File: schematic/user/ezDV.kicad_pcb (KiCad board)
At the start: 4 copper layers, 64.8 x 69.9 mm, 92 parts, among them J1 TYPE-C-31-M-04, J2 Radio_Jack, J3 User_Jack, J4 I2C Breakout, J5 PTT Breakout, Q1 AO3401A, Q2 AO3401A, Q3 MBT3904DW1T1, Q4 MBT3904DW1T1, Q5 MBT3904DW1T1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

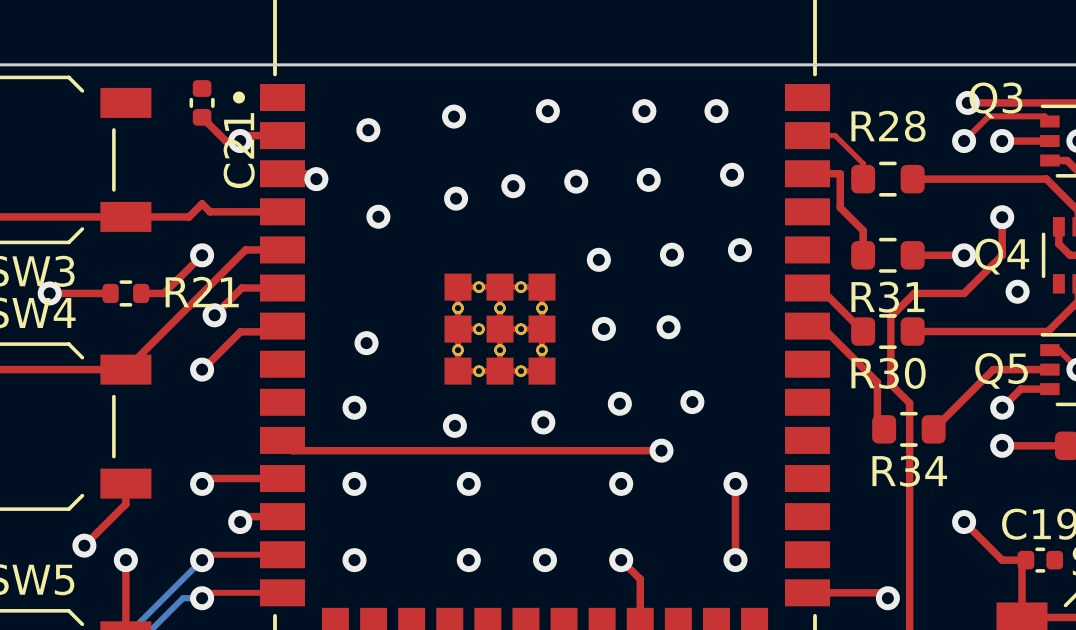
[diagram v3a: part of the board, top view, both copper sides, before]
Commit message: v0.5 board: move PTT and NET GPIOs to RTC domain.
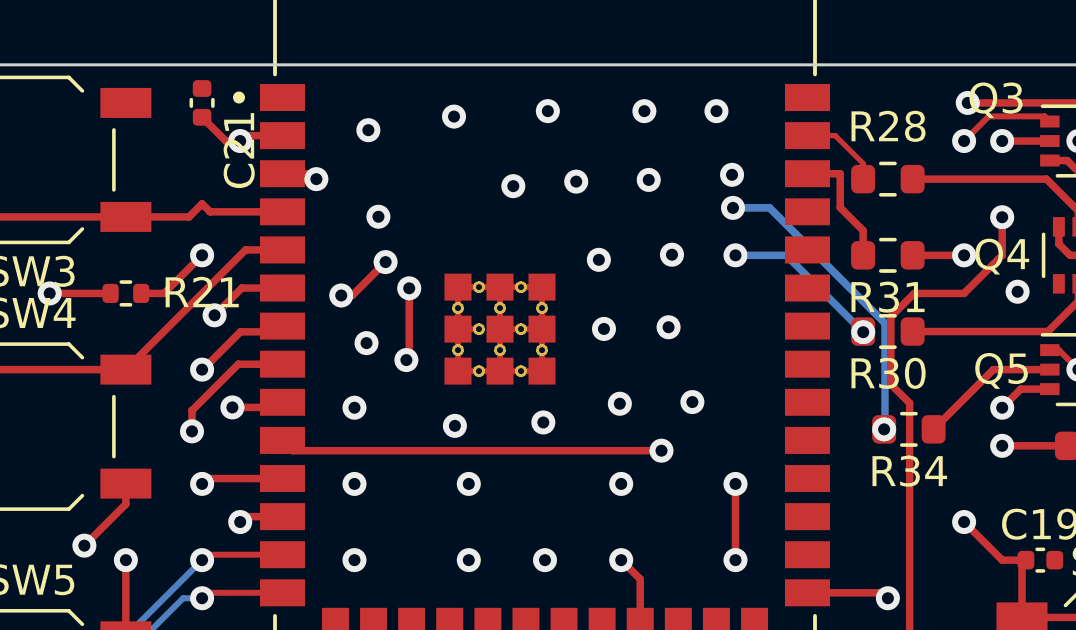
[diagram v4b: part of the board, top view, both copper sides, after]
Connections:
- R30 pad 2: GPIO42_NET_LED -> GPIO16_NET_LED
- R34 pad 2: GPIO41_PTT_LED -> GPIO15_PTT_LED
- U5 pad 34: GPIO41_PTT_LED -> unconnected-(U5-Pad34)
- U5 pad 35: GPIO42_NET_LED -> unconnected-(U5-Pad35)
- U5 pad 8: unconnected-(U5-Pad8) -> GPIO15_PTT_LED
- U5 pad 9: unconnected-(U5-Pad9) -> GPIO16_NET_LED
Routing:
- net GPIO15_PTT_LED: track 0.00 -> 36.0 mm, vias 0 -> 5
- net GPIO16_NET_LED: track 0.00 -> 28.2 mm, vias 0 -> 5
- net GPIO41_PTT_LED: track 4.77 -> 0.00 mm
- net GPIO42_NET_LED: track 2.46 -> 0.00 mm
- net GND: vias 237 -> 235
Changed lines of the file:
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@@
   (net 71 "GPIO7_VOL_DOWN")
   (net 72 "GPIO1_SYNC_LED")
-  (net 73 "GPIO42_NET_LED")
+  (net 73 "GPIO16_NET_LED")
   (net 74 "GPIO2_OVL_LED")
-  (net 75 "GPIO41_PTT_LED")
+  (net 75 "GPIO15_PTT_LED")
   (net 76 "GPIO0_BOOT")
   (net 77 "GPIO8_BAT_ALERT")
-  (net 78 "unconnected-(U5-Pad9)")
+  (net 78 "unconnected-(U5-Pad34)")
   (net 79 "GPIO17_PERIPH_PWR")
   (net 80 "unconnected-(J1-PadS1)")
@@
   (net 96 "TP4056_NTC")
   (net 97 "GPIO18_BOARD_TEMP")
-  (net 98 "unconnected-(U5-Pad8)")
+  (net 98 "unconnected-(U5-Pad35)")
   (net 99 "unconnected-(U5-Pad25)")
   (footprint "Resistor_SMD:R_0603_1608Metric" (layer "F.Cu")
@@
       (net 49 "Net-(Q4-Pad5)") (pintype "passive"))
     (pad "2" smd roundrect (at 0.825 0 180) (size 0.8 0.95) (layers "F.Cu" "F.Paste" "F.Mask") (roundrect_rratio 0.25)
-      (net 73 "GPIO42_NET_LED") (pintype "passive"))
+      (net 73 "GPIO16_NET_LED") (pintype "passive"))
     (model "${KICAD6_3DMODEL_DIR}/Resistor_SMD.3dshapes/R_0603_1608Metric.wrl"
       (offset (xyz 0 0 0))
@@
       (net 71 "GPIO7_VOL_DOWN") (pinfunction "IO7") (pintype "bidirectional"))
     (pad "8" smd rect locked (at -8.75 3.63) (size 1.5 0.9) (layers "F.Cu" "F.Paste" "F.Mask")
-      (net 98 "unconnected-(U5-Pad8)") (pinfunction "IO15") (pintype "bidirectional+no_connect"))
+      (net 75 "GPIO15_PTT_LED") (pinfunction "IO15") (pintype "bidirectional"))
     (pad "9" smd rect locked (at -8.75 4.9) (size 1.5 0.9) (layers "F.Cu" "F.Paste" "F.Mask")
-      (net 78 "unconnected-(U5-Pad9)") (pinfunction "IO16") (pintype "bidirectional+no_connect"))
+      (net 73 "GPIO16_NET_LED") (pinfunction "IO16") (pintype "bidirectional"))
     (pad "10" smd rect locked (at -8.75 6.17) (size 1.5 0.9) (layers "F.Cu" "F.Paste" "F.Mask")
       (net 79 "GPIO17_PERIPH_PWR") (pinfunction "IO17") (pintype "bidirectional"))
@@
       (net 95 "unconnected-(U5-Pad33)") (pinfunction "IO40") (pintype "bidirectional+no_connect"))
     (pad "34" smd rect locked (at 8.75 2.36) (size 1.5 0.9) (layers "F.Cu" "F.Paste" "F.Mask")
-      (net 75 "GPIO41_PTT_LED") (pinfunction "IO41") (pintype "bidirectional"))
+      (net 78 "unconnected-(U5-Pad34)") (pinfunction "IO41") (pintype "bidirectional+no_connect"))
     (pad "35" smd rect locked (at 8.75 1.09) (size 1.5 0.9) (layers "F.Cu" "F.Paste" "F.Mask")
-      (net 73 "GPIO42_NET_LED") (pinfunction "IO42") (pintype "bidirectional"))
+      (net 98 "unconnected-(U5-Pad35)") (pinfunction "IO42") (pintype "bidirectional+no_connect"))
     (pad "36" smd rect locked (at 8.75 -0.18) (size 1.5 0.9) (layers "F.Cu" "F.Paste" "F.Mask")
       (net 86 "unconnected-(U5-Pad36)") (pinfunction "RXD0") (pintype "bidirectional+no_connect"))
@@
       (net 50 "Net-(Q5-Pad2)") (pintype "passive"))
     (pad "2" smd roundrect (at 0.825 0 180) (size 0.8 0.95) (layers "F.Cu" "F.Paste" "F.Mask") (roundrect_rratio 0.25)
-      (net 75 "GPIO41_PTT_LED") (pintype "passive"))
+      (net 75 "GPIO15_PTT_LED") (pintype "passive"))
     (model "${KICAD6_3DMODEL_DIR}/Resistor_SMD.3dshapes/R_0603_1608Metric.wrl"
       (offset (xyz 0 0 0))
@@
   (via (at 90.17 107.95) (size 0.8) (drill 0.4) (layers "F.Cu" "B.Cu") (free) (net 2))
   (via (at 82.329331 117.655234) (size 0.8) (drill 0.4) (layers "F.Cu" "B.Cu") (free) (net 2))
-  (via (at 80.159472 74.758624) (size 0.8) (drill 0.4) (layers "F.Cu" "B.Cu") (free) (net 2))
   (via (at 47.324831 88.987026) (size 0.8) (drill 0.4) (layers "F.Cu" "B.Cu") (free) (net 2))
   (via (at 104.265111 94.610548) (size 0.8) (drill 0.4) (layers "F.Cu" "B.Cu") (free) (net 2))
@@
   (via (at 95.184712 114.038378) (size 0.8) (drill 0.4) (layers "F.Cu" "B.Cu") (free) (net 2))
   (via (at 55.88 105.41) (size 0.8) (drill 0.4) (layers "F.Cu" "B.Cu") (free) (net 2))
-  (via (at 70.695662 73.039648) (size 0.8) (drill 0.4) (layers "F.Cu" "B.Cu") (free) (net 2))
   (via (at 76.179226 132.09359) (size 0.8) (drill 0.4) (layers "F.Cu" "B.Cu") (free) (net 2))
   (via (at 92.944297 122.664323) (size 0.8) (drill 0.4) (layers "F.Cu" "B.Cu") (free) (net 2))
@@
   (segment (start 83.335 70.94) (end 84.265 71.87) (width 0.175) (layer "F.Cu") (net 72))
   (segment (start 82.41 70.94) (end 83.335 70.94) (width 0.175) (layer "F.Cu") (net 72))
-  (segment (start 82.815 76.02) (end 84.265 77.47) (width 0.25) (layer "F.Cu") (net 73))
-  (segment (start 82.41 76.02) (end 82.815 76.02) (width 0.25) (layer "F.Cu") (net 73))
+  (segment (start 64.739894 80.000106) (end 64.91 79.83) (width 0.25) (layer "F.Cu") (net 73))
+  (segment (start 69.133734 76.029615) (end 69.133734 78.327485) (width 0.25) (layer "F.Cu") (net 73))
+  (segment (start 63.240008 80.000106) (end 64.739894 80.000106) (width 0.25) (layer "F.Cu") (net 73))
+  (segment (start 69.133734 78.327485) (end 69.039738 78.421481) (width 0.25) (layer "F.Cu") (net 73))
+  (via (at 80.01 74.93) (size 0.8) (drill 0.4) (layers "F.Cu" "B.Cu") (free) (net 73))
+  (via (at 84.267299 77.492096) (size 0.8) (drill 0.4) (layers "F.Cu" "B.Cu") (net 73))
+  (via (at 69.133734 76.029615) (size 0.8) (drill 0.4) (layers "F.Cu" "B.Cu") (free) (net 73))
+  (via (at 69.039738 78.421481) (size 0.8) (drill 0.4) (layers "F.Cu" "B.Cu") (net 73))
+  (via (at 63.240008 80.000106) (size 0.8) (drill 0.4) (layers "F.Cu" "B.Cu") (free) (net 73))
+  (segment (start 69.133734 75.539111) (end 70.488102 74.184743) (width 0.25) (layer "In2.Cu") (net 73))
+  (segment (start 80.01 74.93) (end 79.390017 74.93) (width 0.25) (layer "In2.Cu") (net 73))
+  (segment (start 63.955114 79.285) (end 68.176219 79.285) (width 0.25) (layer "In2.Cu") (net 73))
+  (segment (start 63.240008 80.000106) (end 63.955114 79.285) (width 0.25) (layer "In2.Cu") (net 73))
+  (segment (start 70.488102 74.184743) (end 78.64476 74.184743) (width 0.25) (layer "In2.Cu") (net 73))
+  (segment (start 68.176219 79.285) (end 69.039738 78.421481) (width 0.25) (layer "In2.Cu") (net 73))
+  (segment (start 69.133734 76.029615) (end 69.133734 75.539111) (width 0.25) (layer "In2.Cu") (net 73))
+  (segment (start 79.390017 74.93) (end 78.64476 74.184743) (width 0.25) (layer "In2.Cu") (net 73))
+  (segment (start 80.01 74.93) (end 81.705203 74.93) (width 0.25) (layer "B.Cu") (net 73))
+  (segment (start 81.705203 74.93) (end 84.267299 77.492096) (width 0.25) (layer "B.Cu") (net 73))
   (segment (start 83.501636 72.21) (end 83.501636 73.341636) (width 0.25) (layer "F.Cu") (net 74))
   (segment (start 83.501636 73.341636) (end 84.265 74.105) (width 0.25) (layer "F.Cu") (net 74))
   (segment (start 82.41 72.21) (end 83.501636 72.21) (width 0.25) (layer "F.Cu") (net 74))
   (segment (start 84.265 74.105) (end 84.265 74.93) (width 0.25) (layer "F.Cu") (net 74))
-  (segment (start 82.41 77.29) (end 82.867538 77.29) (width 0.25) (layer "F.Cu") (net 75))
-  (segment (start 82.867538 77.29) (end 84.74 79.162462) (width 0.25) (layer "F.Cu") (net 75))
-  (segment (start 84.74 79.162462) (end 84.74 80.505778) (width 0.25) (layer "F.Cu") (net 75))
-  (segment (start 84.74 80.505778) (end 84.964769 80.730547) (width 0.25) (layer "F.Cu") (net 75))
+  (segment (start 67.233679 76.268467) (end 68.346848 75.155298) (width 0.25) (layer "F.Cu") (net 75))
+  (segment (start 63.435305 78.56) (end 61.89333 80.101975) (width 0.25) (layer "F.Cu") (net 75))
+  (segment (start 66.868292 76.268467) (end 67.233679 76.268467) (width 0.25) (layer "F.Cu") (net 75))
+  (segment (start 61.89333 80.101975) (end 61.89333 80.798493) (width 0.25) (layer "F.Cu") (net 75))
+  (segment (start 64.91 78.56) (end 63.435305 78.56) (width 0.25) (layer "F.Cu") (net 75))
+  (via (at 66.868292 76.268467) (size 0.8) (drill 0.4) (layers "F.Cu" "B.Cu") (net 75))
+  (via (at 79.926698 73.349072) (size 0.8) (drill 0.4) (layers "F.Cu" "B.Cu") (net 75))
+  (via (at 84.964769 80.730547) (size 0.8) (drill 0.4) (layers "F.Cu" "B.Cu") (net 75))
+  (via (at 61.89333 80.798493) (size 0.8) (drill 0.4) (layers "F.Cu" "B.Cu") (free) (net 75))
+  (via (at 68.346848 75.155298) (size 0.8) (drill 0.4) (layers "F.Cu" "B.Cu") (net 75))
+  (segment (start 70.153074 73.349072) (end 79.926698 73.349072) (width 0.25) (layer "In2.Cu") (net 75))
+  (segment (start 68.346848 75.155298) (end 70.153074 73.349072) (width 0.25) (layer "In2.Cu") (net 75))
+  (segment (start 61.89333 80.798493) (end 61.89333 80.321479) (width 0.25) (layer "In2.Cu") (net 75))
+  (segment (start 65.946342 76.268467) (end 66.868292 76.268467) (width 0.25) (layer "In2.Cu") (net 75))
+  (segment (start 61.89333 80.321479) (end 65.946342 76.268467) (width 0.25) (layer "In2.Cu") (net 75))
+  (segment (start 84.964769 80.730547) (end 84.992299 80.703017) (width 0.25) (layer "B.Cu") (net 75))
+  (segment (start 84.992299 80.703017) (end 84.992299 77.191791) (width 0.25) (layer "B.Cu") (net 75))
+  (segment (start 84.992299 77.191791) (end 81.14958 73.349072) (width 0.25) (layer "B.Cu") (net 75))
+  (segment (start 81.14958 73.349072) (end 79.926698 73.349072) (width 0.25) (layer "B.Cu") (net 75))
   (segment (start 82.41 86.18) (end 84.91 86.18) (width 0.25) (layer "F.Cu") (net 76))
   (segment (start 84.91 86.18) (end 85.09 86.36) (width 0.25) (layer "F.Cu") (net 76))

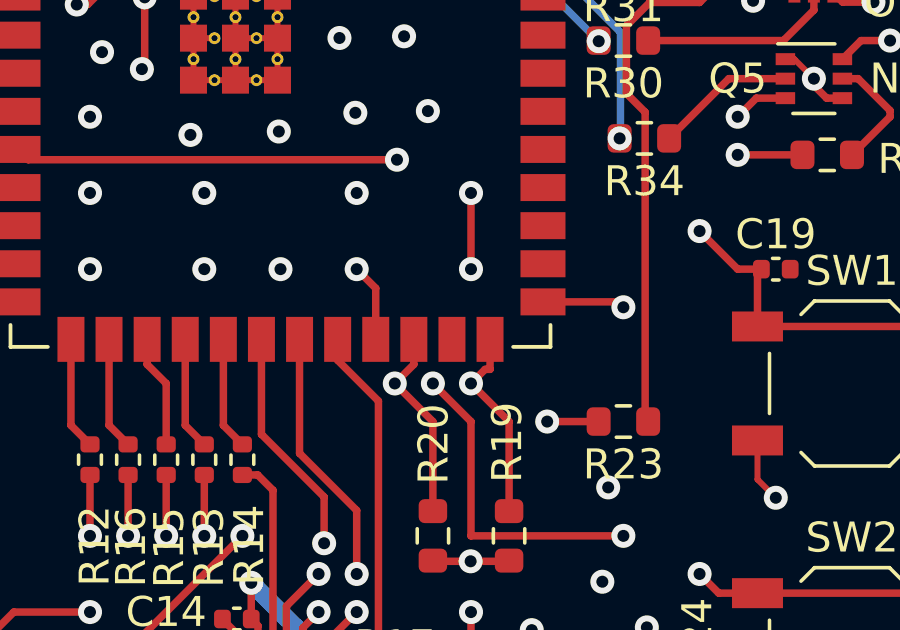
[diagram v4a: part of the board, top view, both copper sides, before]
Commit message: v0.5 board: move SCL to GPIO 48 as 45 is a ESP32 strapping pin.
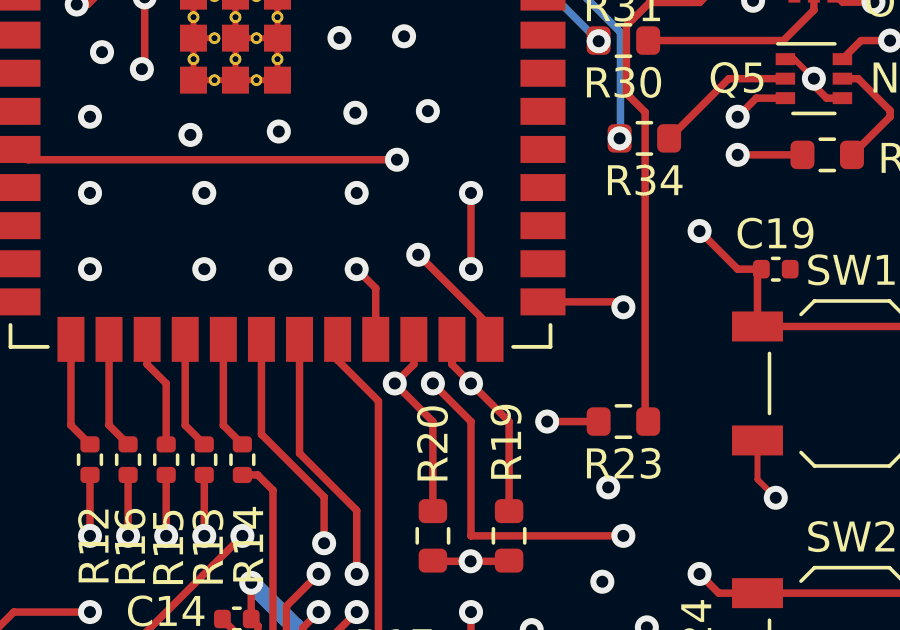
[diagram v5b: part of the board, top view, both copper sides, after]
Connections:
- J4 pad 3: GPIO45_SCL -> GPIO48_SCL
- R19 pad 2: GPIO45_SCL -> GPIO48_SCL
- U2 pad 7: GPIO45_SCL -> GPIO48_SCL
- U4 pad 9: GPIO45_SCL -> GPIO48_SCL
- U5 pad 25: unconnected-(U5-Pad25) -> GPIO48_SCL
- U5 pad 26: GPIO45_SCL -> GND
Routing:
- net GPIO45_SCL: track 58.5 -> 0.00 mm, vias 5 -> 0
- net GPIO48_SCL: track 0.00 -> 58.4 mm, vias 0 -> 4
- net GND: track 85.9 -> 89.8 mm, vias 235 -> 237

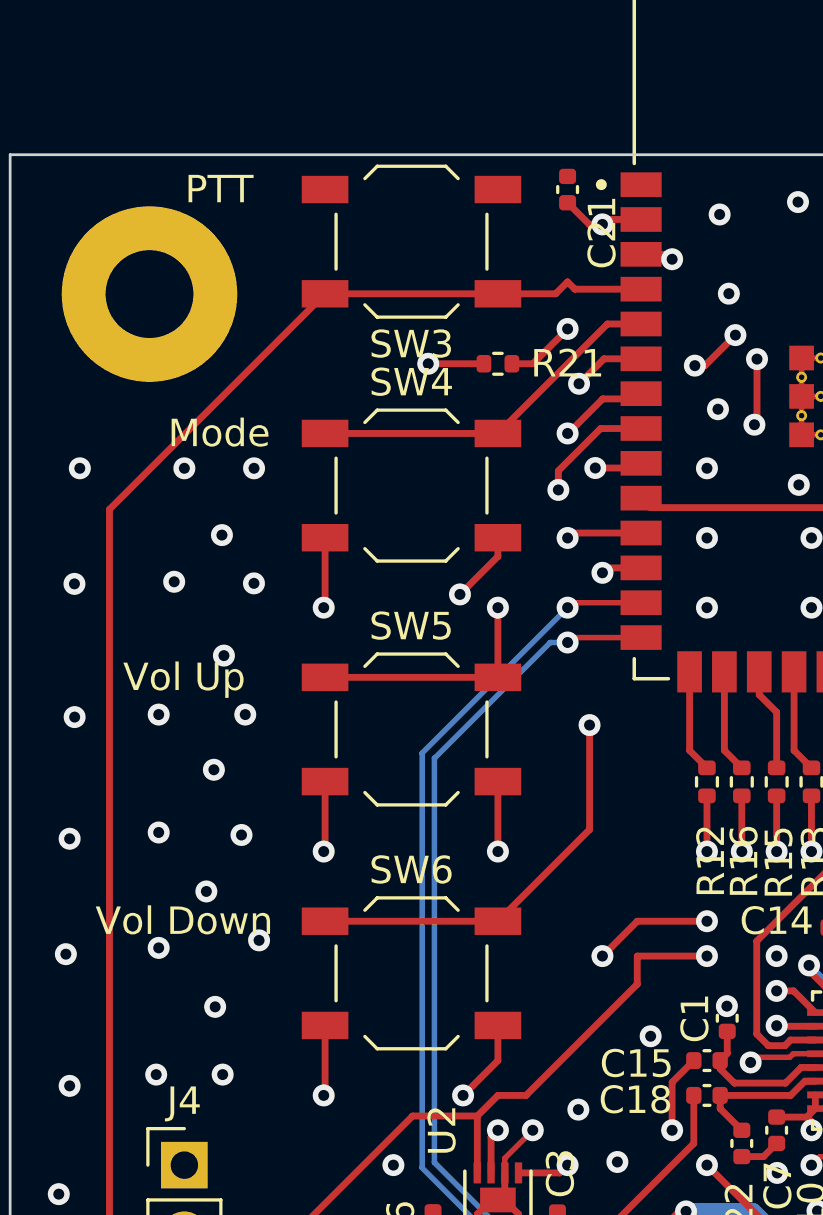
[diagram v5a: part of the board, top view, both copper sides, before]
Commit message: v0.5 board: use taller buttons to hopefully avoid need to build buttons into enclosure.
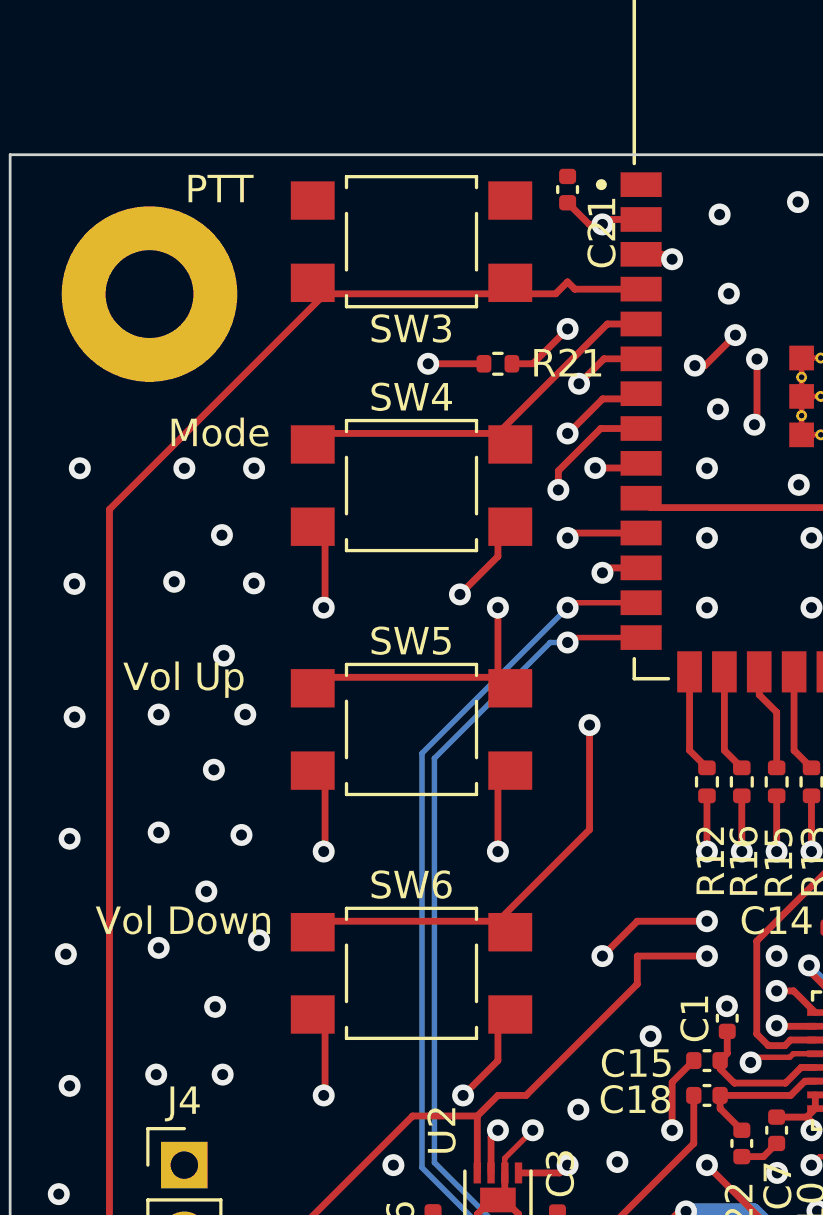
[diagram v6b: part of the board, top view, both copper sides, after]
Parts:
- SW3, SW4, SW5, SW6: footprint Button_Switch_SMD:SW_SPST_TL3342 -> Button_Switch_SMD:SW_SPST_TL3305C
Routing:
- net GPIO48_SCL: vias 4 -> 5
- net GND: vias 237 -> 236
